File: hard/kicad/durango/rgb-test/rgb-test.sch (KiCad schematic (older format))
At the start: 21 parts, among them J1 SCART, SW1 TEST, U1 74HCT4040, U18 74HC85, U2 74HC4040, U20 74HC85, U3 74HC21, U4 74HC02, U5 74HC245, U6 74HC86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

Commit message: annotate and improve RGB tester
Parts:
- R4: value 1K -> 1K2
- R5: value 150 -> 180
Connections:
- net +5V: now also U3.13; no longer U3.1
- net FEND: now also U3.6; no longer U3.8
- net H2: now also U3.9; no longer U3.2
- net LEND: now also U3.8; no longer U3.6
- net S_G: now also J1.11 (Pin_11), R1.1; no longer J1.15 (Pin_15), R2.1
- net V0: now also U3.1; no longer U3.13
- net VA1: now also U3.12; no longer U3.5
- net ~DEH: now also U3.10; no longer U3.4
- net ~DEV: now also U3.4; no longer U3.10
- net at U2.5 (Q3), U20.12 (A1): now also U3.5; no longer U3.9
- net at U2.3 (Q4), U20.13 (A2): now also U3.2; no longer U3.12
- net FB: now reaches J1.16 (Pin_16), SW1.1 (A)
- new net S_R: J1.15 (Pin_15), R2.1
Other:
- note added: "74AC might be fast enough for nominal f."
- note added: "Horizontal/Vertical pattern choice,\nmay be connected to any counter output"
- note added: "may be supressed,\nfor buffering only"
- note added: "or +5V for\nnominal f."
- note added: "or 24 MHz\nfor nominal f."
- note added: "or higher,\nup to 360"
- note added: "or lower, down to 470 ohm"
- note added: "press to disable RGB\n(dark grey square)"
- note added: "these may be supressed,\nfor buffering only"
- moved on the sheet: U3A, U3B
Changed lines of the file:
@@
 L power:+5V #PWR0120
 U 1 1 6080689B
-P 4650 3900
-F 0 "#PWR0120" H 4650 3750 50  0001 C CNN
-F 1 "+5V" V 4700 3950 50  0000 L CNN
-F 2 "" H 4650 3900 50  0001 C CNN
-F 3 "" H 4650 3900 50  0001 C CNN
-	1    4650 3900
-	0    -1   -1   0
+P 4650 3300
+F 0 "#PWR0120" H 4650 3150 50  0001 C CNN
+F 1 "+5V" H 4700 3350 50  0000 L CNN
+F 2 "" H 4650 3300 50  0001 C CNN
+F 3 "" H 4650 3300 50  0001 C CNN
+	1    4650 3300
+	1    0    0    -1
 $EndComp
 $Comp
@@
 P 6800 5200
 F 0 "R4" V 6700 5200 50  0000 C CNN
-F 1 "1K" V 6800 5200 50  0000 C CNN
+F 1 "1K2" V 6800 5200 50  0000 C CNN
 F 2 "Resistor_THT:R_Axial_DIN0207_L6.3mm_D2.5mm_P2.54mm_Vertical" V 6730 5200 50  0001 C CNN
 F 3 "~" H 6800 5200 50  0001 C CNN
@@
 U 1 1 615F5223
 P 8950 5700
-F 0 "R5" V 9050 5700 50  0000 C CNN
-F 1 "150" V 8950 5700 50  0000 C CNN
+F 0 "R5" V 8850 5700 50  0000 C CNN
+F 1 "180" V 8950 5700 50  0000 C CNN
 F 2 "Resistor_THT:R_Axial_DIN0309_L9.0mm_D3.2mm_P2.54mm_Vertical" V 8880 5700 50  0001 C CNN
 F 3 "~" H 8950 5700 50  0001 C CNN
@@
 Wire Wire Line
 	9950 2550 9750 2550
-Wire Wire Line
-	4300 2450 5450 2450
-Wire Wire Line
-	5450 2450 5450 3400
 Wire Wire Line
 	4650 4400 4950 4400
@@
 $EndComp
 Wire Wire Line
-	3600 2750 4100 2750
-Text Label 3800 2750 0    50   ~ 0
+	3600 2550 4250 2550
+Text Label 3800 2550 0    50   ~ 0
 VA1
-Wire Wire Line
-	3600 2550 5650 2550
-Connection ~ 5650 2550
 Wire Wire Line
 	3600 2650 5750 2650
@@
 Text Label 3800 2650 0    50   ~ 0
 ~LINE
-Text Label 3800 2550 0    50   ~ 0
+Text Label 3800 2750 0    50   ~ 0
 VA5
 Wire Wire Line
@@
 L 74xx:74LS21 U3
 U 1 1 615D7357
+P 7600 3800
+F 0 "U3" V 7700 3550 50  0000 C CNN
+F 1 "74HC21" V 7800 3550 50  0000 C CNN
+F 2 "Package_DIP:DIP-14_W7.62mm_Socket" H 7600 3800 50  0001 C CNN
+F 3 "http://www.ti.com/lit/gpn/sn74LS21" H 7600 3800 50  0001 C CNN
+	1    7600 3800
+	0    1    1    0
+$EndComp
+$Comp
+L 74xx:74LS21 U3
+U 2 1 615EA142
 P 3300 2600
-F 0 "U3" H 3550 2550 50  0000 C CNN
-F 1 "74HC21" H 3550 2450 50  0000 C CNN
+F 0 "U3" H 3600 2750 50  0000 R CNN
+F 1 "74HC21" H 3650 2850 50  0000 R CNN
 F 2 "Package_DIP:DIP-14_W7.62mm_Socket" H 3300 2600 50  0001 C CNN
 F 3 "http://www.ti.com/lit/gpn/sn74LS21" H 3300 2600 50  0001 C CNN
-	1    3300 2600
-	-1   0    0    -1
-$EndComp
-$Comp
-L 74xx:74LS21 U3
-U 2 1 615EA142
-P 7600 3800
-F 0 "U3" V 7650 4200 50  0000 R CNN
-F 1 "74HC21" V 7750 4200 50  0000 R CNN
-F 2 "Package_DIP:DIP-14_W7.62mm_Socket" H 7600 3800 50  0001 C CNN
-F 3 "http://www.ti.com/lit/gpn/sn74LS21" H 7600 3800 50  0001 C CNN
-	2    7600 3800
-	0    -1   1    0
+	2    3300 2600
+	-1   0    0    1
 $EndComp
 Wire Wire Line
@@
 NoConn ~ 2500 1100
 Wire Wire Line
-	2500 1600 4100 1600
-Wire Wire Line
-	4100 1600 4100 2750
-Wire Wire Line
-	2500 1800 4300 1800
-Wire Wire Line
-	4300 1800 4300 2450
+	2500 1600 4250 1600
+Wire Wire Line
+	4250 1600 4250 2550
+Wire Wire Line
+	2500 1800 5450 1800
 Wire Wire Line
 	2500 1900 5550 1900
@@
 Wire Wire Line
 	2500 2000 5650 2000
-Wire Wire Line
-	5650 2000 5650 2550
 Wire Wire Line
 	2500 2100 5750 2100
@@
 	5750 2100 5750 2150
 NoConn ~ 2500 2200
-Wire Wire Line
-	5650 2550 5650 3400
 Connection ~ 2000 800
 Wire Wire Line
@@
 Text Label 7550 5700 0    50   ~ 0
 S_R
-Text Label 7550 6000 0    50   ~ 0
+Text Label 7650 5900 1    50   ~ 0
 S_G
 Text Label 7550 6200 0    50   ~ 0
@@
 Text Label 8300 5500 0    50   ~ 0
 COMP
+Text Notes 8500 5050 0    50   ~ 0
+or lower, down to 470 ohm
+Text Notes 8700 5900 0    50   ~ 0
+or higher,\nup to 360
+Text Notes 3850 6400 0    50   ~ 10
+Horizontal/Vertical pattern choice,\nmay be connected to any counter output
+Text Notes 9300 2100 0    50   ~ 0
+may be supressed,\nfor buffering only
+Text Notes 3650 4650 0    50   ~ 0
+these may be supressed,\nfor buffering only
+Text Notes 500  1400 0    50   Italic 0
+or 24 MHz\nfor nominal f.
+Text Notes 3800 2450 0    50   Italic 0
+or +5V for\nnominal f.
+Wire Wire Line
+	5650 2000 5650 2750
+Wire Wire Line
+	5650 2750 3600 2750
+Connection ~ 5650 2750
+Wire Wire Line
+	5650 2750 5650 3400
+Wire Wire Line
+	5450 1800 5450 3400
+Text Notes 2300 750  0    50   Italic 0
+74AC might be fast enough for nominal f.
+Text Notes 8550 5550 0    50   ~ 10
+press to disable RGB\n(dark grey square)
+Text Label 8350 5700 0    50   ~ 0
+FB
+Connection ~ 4650 3300
 $EndSCHEMATC

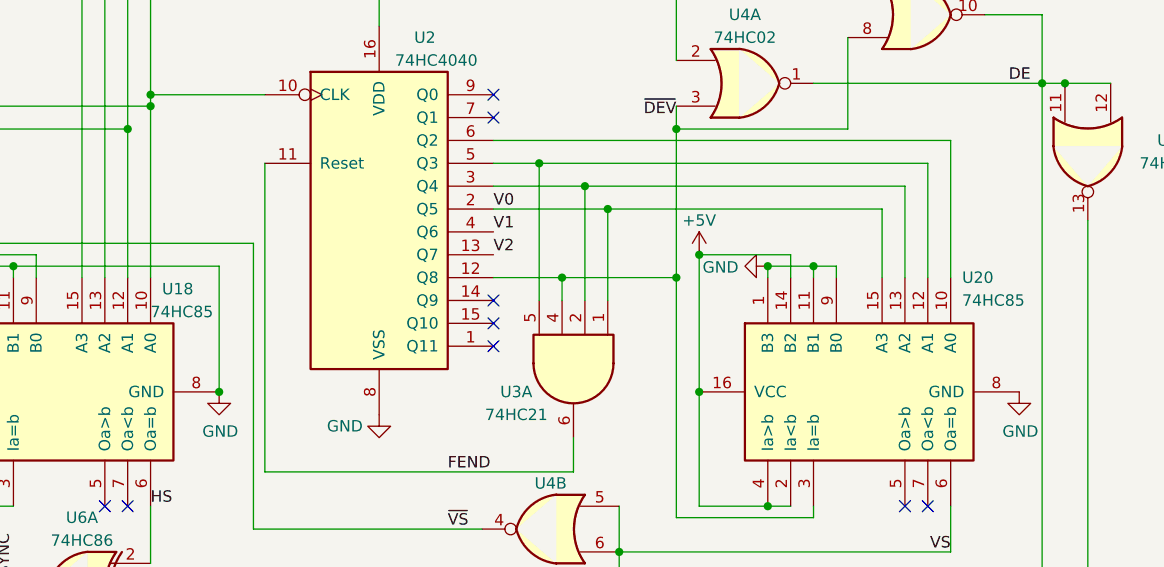
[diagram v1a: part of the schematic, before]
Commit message: rename HC85 from RGB tester
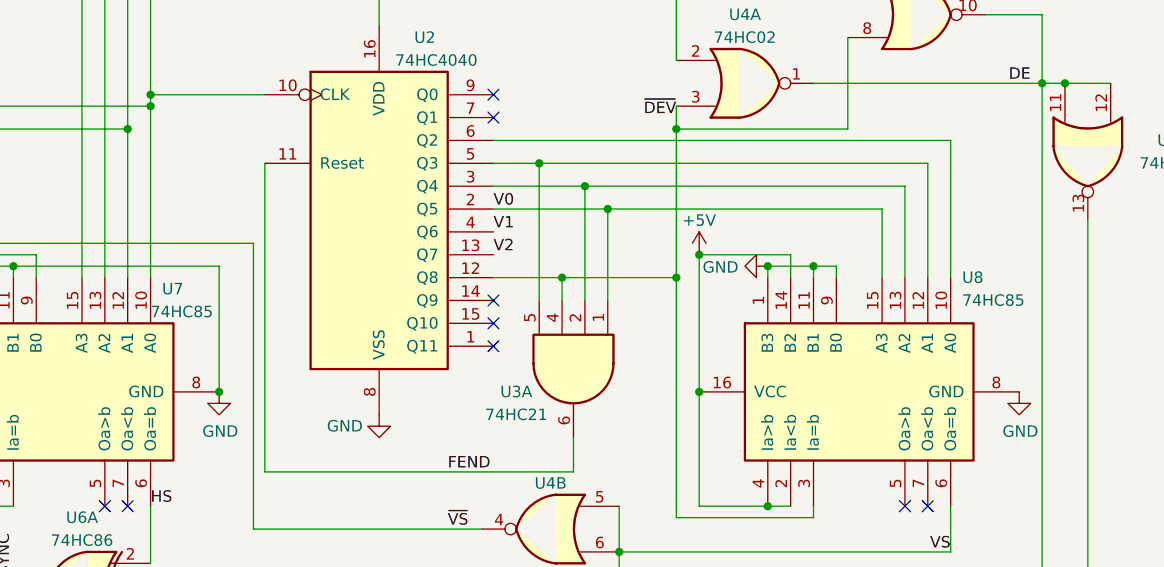
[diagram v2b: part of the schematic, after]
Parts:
- renumbered U18 to U7, U20 to U8
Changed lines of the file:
@@
 $EndComp
 $Comp
-L 74xx:74LS85 U18
+L 74xx:74LS85 U7
 U 1 1 607EF60C
 P 5350 3900
-F 0 "U18" V 4900 3450 50  0000 R CNN
+F 0 "U7" V 4900 3450 50  0000 R CNN
 F 1 "74HC85" V 5000 3500 50  0000 R CNN
 F 2 "Package_DIP:DIP-16_W7.62mm_Socket" H 5350 3900 50  0001 C CNN
@@
 $EndComp
 $Comp
-L 74xx:74LS85 U20
+L 74xx:74LS85 U8
 U 1 1 607F05F3
 P 8850 3900
-F 0 "U20" V 8350 3450 50  0000 R CNN
+F 0 "U8" V 8350 3450 50  0000 R CNN
 F 1 "74HC85" V 8450 3450 50  0000 R CNN
 F 2 "Package_DIP:DIP-16_W7.62mm_Socket" H 8850 3900 50  0001 C CNN

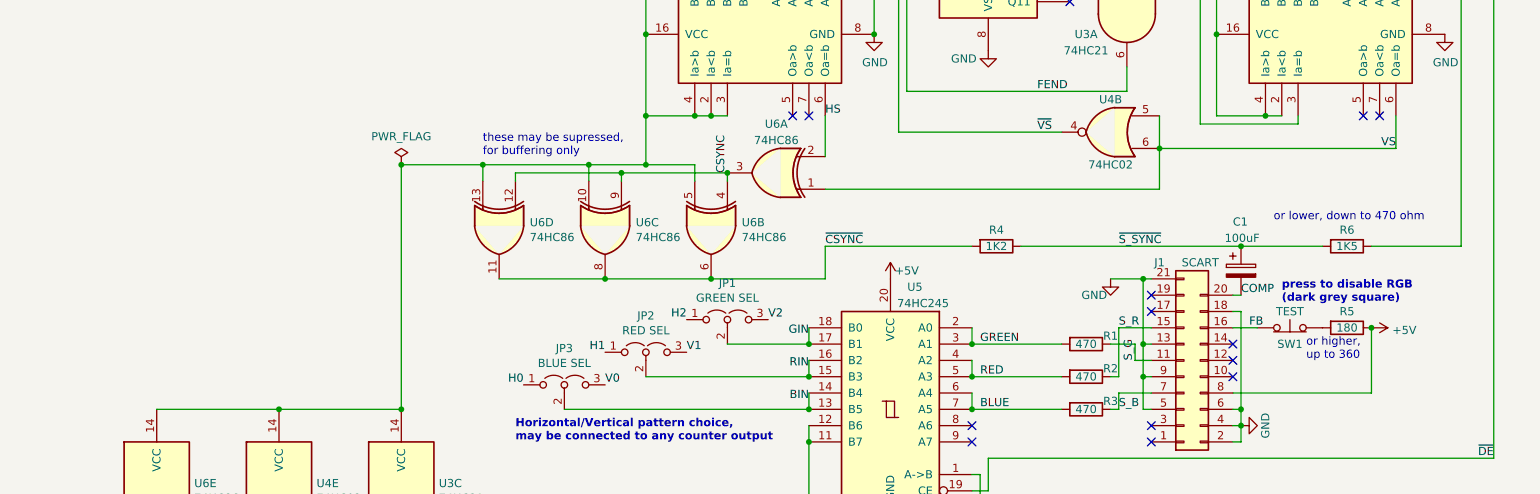
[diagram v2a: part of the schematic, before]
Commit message: PCB for RGB tester
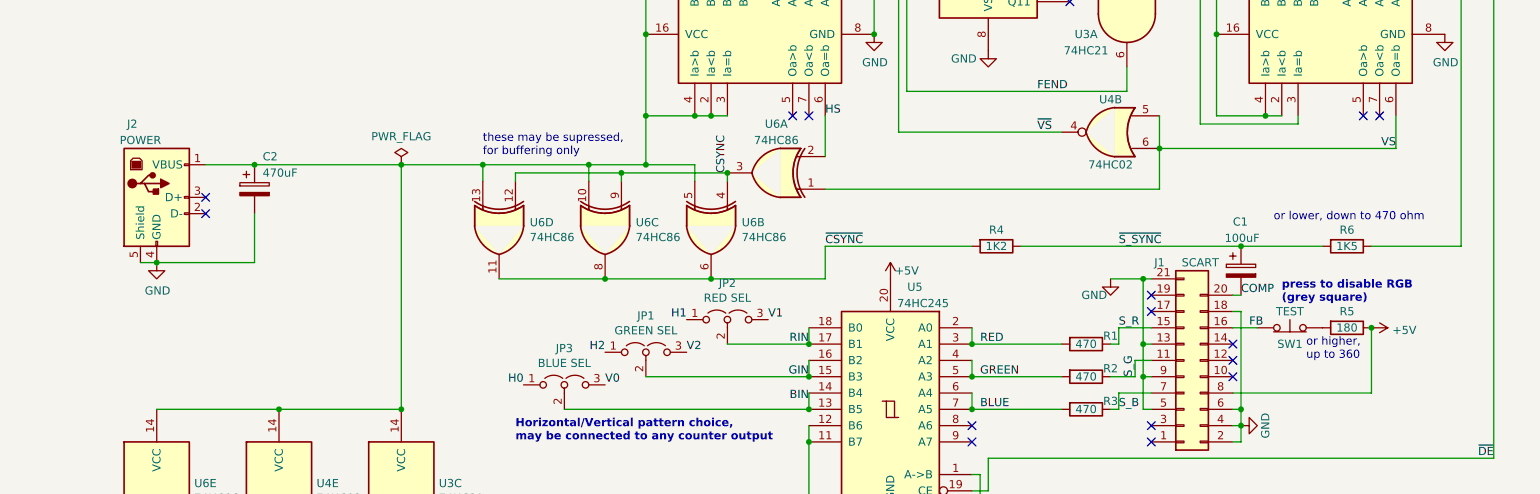
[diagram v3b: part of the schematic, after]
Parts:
- added C2: 470uF, Capacitor_THT:CP_Radial_D6.3mm_P2.50mm, symbol Device:CP
- added J2: POWER, Connector_USB:USB_B_OST_USB-B1HSxx_Horizontal, symbol Connector:USB_B
- JP1, JP2, JP3: footprint (none) -> Connector_PinHeader_2.54mm:PinHeader_1x03_P2.54mm_Vertical
- R6: footprint (none) -> Resistor_THT:R_Axial_DIN0207_L6.3mm_D2.5mm_P2.54mm_Vertical
- SW1: footprint (none) -> Button_Switch_THT:SW_PUSH_6mm
- U3, U4, U6: footprint (none) -> Package_DIP:DIP-14_W7.62mm_Socket
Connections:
- net +5V: now also C2.1, J2.1 (VBUS)
- net GIN: now also U5.15 (B3), U5.16 (B2); no longer U5.17 (B1), U5.18 (B0)
- net GND: now also C2.2, J2.4 (GND), J2.5 (Shield)
- net GREEN: now also R2.2, U5.4 (A2), U5.5 (A3); no longer R1.2, U5.2 (A0), U5.3 (A1)
- net RED: now also R1.2, U5.2 (A0), U5.3 (A1); no longer R2.2, U5.4 (A2), U5.5 (A3)
- net RIN: now also U5.17 (B1), U5.18 (B0); no longer U5.15 (B3), U5.16 (B2)
- net S_G: now also R2.1; no longer R1.1
- net S_R: now also R1.1; no longer R2.1
- no-connect marks 25 -> 27
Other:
- note added: "press to disable RGB\n(grey square)"
- note removed: "press to disable RGB\n(dark grey square)"
- moved on the sheet: JP1, JP2
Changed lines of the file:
@@
 	7550 5700 7750 5700
-Wire Wire Line
-	7650 5800 7500 5800
 Wire Wire Line
 	7650 5900 7750 5900
@@
 $EndComp
 Wire Wire Line
-	7650 5900 7650 5800
-Wire Wire Line
-	7550 5700 7550 6000
-Wire Wire Line
-	7550 6000 7500 6000
+	7650 5900 7650 6000
+Wire Wire Line
+	7650 6000 7500 6000
 Wire Wire Line
 	7550 6100 7550 6200
@@
 Wire Wire Line
 	9850 6500 9850 3150
+Text Label 6700 6000 0    50   ~ 0
+GREEN
 Text Label 6700 5800 0    50   ~ 0
-GREEN
-Text Label 6700 6000 0    50   ~ 0
 RED
 Text Label 6700 6200 0    50   ~ 0
@@
 Text Label 7550 5200 0    50   ~ 0
 ~S_SYNC
-Text Label 5650 5750 2    50   ~ 0
+Text Label 5650 6000 2    50   ~ 0
 GIN
-Text Label 5650 5950 2    50   ~ 0
+Text Label 5650 5800 2    50   ~ 0
 RIN
 Text Label 5650 6150 2    50   ~ 0
@@
 Text Label 7550 5700 0    50   ~ 0
 S_R
-Text Label 7650 5900 1    50   ~ 0
+Text Label 7650 6000 1    50   ~ 0
 S_G
 Text Label 7550 6200 0    50   ~ 0
@@
 F 0 "U6" H 5450 4450 50  0000 C CNN
 F 1 "74HC86" H 5450 4550 50  0000 C CNN
-F 2 "" H 5450 4750 50  0001 C CNN
+F 2 "Package_DIP:DIP-14_W7.62mm_Socket" H 5450 4750 50  0001 C CNN
 F 3 "http://www.ti.com/lit/gpn/sn74HC86" H 5450 4750 50  0001 C CNN
 	1    5450 4750
@@
 F 0 "U6" V 5004 5288 50  0000 L CNN
 F 1 "74HC86" V 5095 5288 50  0000 L CNN
-F 2 "" H 5050 5100 50  0001 C CNN
+F 2 "Package_DIP:DIP-14_W7.62mm_Socket" H 5050 5100 50  0001 C CNN
 F 3 "http://www.ti.com/lit/gpn/sn74HC86" H 5050 5100 50  0001 C CNN
 	2    5050 5100
@@
 F 0 "U6" V 4354 5288 50  0000 L CNN
 F 1 "74HC86" V 4445 5288 50  0000 L CNN
-F 2 "" H 4400 5100 50  0001 C CNN
+F 2 "Package_DIP:DIP-14_W7.62mm_Socket" H 4400 5100 50  0001 C CNN
 F 3 "http://www.ti.com/lit/gpn/sn74HC86" H 4400 5100 50  0001 C CNN
 	3    4400 5100
@@
 F 0 "U6" V 3704 5288 50  0000 L CNN
 F 1 "74HC86" V 3795 5288 50  0000 L CNN
-F 2 "" H 3750 5100 50  0001 C CNN
+F 2 "Package_DIP:DIP-14_W7.62mm_Socket" H 3750 5100 50  0001 C CNN
 F 3 "http://www.ti.com/lit/gpn/sn74HC86" H 3750 5100 50  0001 C CNN
 	4    3750 5100
@@
 F 0 "U6" H 1880 6746 50  0000 L CNN
 F 1 "74HC86" H 1880 6655 50  0000 L CNN
-F 2 "" H 1650 6700 50  0001 C CNN
+F 2 "Package_DIP:DIP-14_W7.62mm_Socket" H 1650 6700 50  0001 C CNN
 F 3 "http://www.ti.com/lit/gpn/sn74HC86" H 1650 6700 50  0001 C CNN
 	5    1650 6700
@@
 F 0 "U4" H 2630 6746 50  0000 L CNN
 F 1 "74HC02" H 2630 6655 50  0000 L CNN
-F 2 "" H 2400 6700 50  0001 C CNN
+F 2 "Package_DIP:DIP-14_W7.62mm_Socket" H 2400 6700 50  0001 C CNN
 F 3 "http://www.ti.com/lit/gpn/sn74hc02" H 2400 6700 50  0001 C CNN
 	5    2400 6700
@@
 F 0 "U3" H 3380 6746 50  0000 L CNN
 F 1 "74HC21" H 3380 6655 50  0000 L CNN
-F 2 "" H 3150 6700 50  0001 C CNN
+F 2 "Package_DIP:DIP-14_W7.62mm_Socket" H 3150 6700 50  0001 C CNN
 F 3 "http://www.ti.com/lit/gpn/sn74LS21" H 3150 6700 50  0001 C CNN
 	3    3150 6700
@@
 	3150 6200 3150 4700
 Wire Wire Line
-	3150 4700 3650 4700
+	3150 4700 2250 4700
 Connection ~ 3150 6200
 Connection ~ 2400 6200
@@
 F 0 "R6" V 8850 5200 50  0000 C CNN
 F 1 "1K5" V 8950 5200 50  0000 C CNN
-F 2 "" V 8880 5200 50  0001 C CNN
+F 2 "Resistor_THT:R_Axial_DIN0207_L6.3mm_D2.5mm_P2.54mm_Vertical" V 8880 5200 50  0001 C CNN
 F 3 "~" H 8950 5200 50  0001 C CNN
 	1    8950 5200
@@
 L Jumper:Jumper_3_Open JP1
 U 1 1 629CB504
+P 4650 5850
+F 0 "JP1" H 4650 6074 50  0000 C CNN
+F 1 "GREEN SEL" H 4650 5983 50  0000 C CNN
+F 2 "Connector_PinHeader_2.54mm:PinHeader_1x03_P2.54mm_Vertical" H 4650 5850 50  0001 C CNN
+F 3 "~" H 4650 5850 50  0001 C CNN
+	1    4650 5850
+	1    0    0    -1
+$EndComp
+$Comp
+L Jumper:Jumper_3_Open JP2
+U 1 1 629CE90F
 P 5150 5650
-F 0 "JP1" H 5150 5874 50  0000 C CNN
-F 1 "GREEN SEL" H 5150 5783 50  0000 C CNN
-F 2 "" H 5150 5650 50  0001 C CNN
+F 0 "JP2" H 5150 5874 50  0000 C CNN
+F 1 "RED SEL" H 5150 5783 50  0000 C CNN
+F 2 "Connector_PinHeader_2.54mm:PinHeader_1x03_P2.54mm_Vertical" H 5150 5650 50  0001 C CNN
 F 3 "~" H 5150 5650 50  0001 C CNN
 	1    5150 5650
-	1    0    0    -1
-$EndComp
-$Comp
-L Jumper:Jumper_3_Open JP2
-U 1 1 629CE90F
-P 4650 5850
-F 0 "JP2" H 4650 6074 50  0000 C CNN
-F 1 "RED SEL" H 4650 5983 50  0000 C CNN
-F 2 "" H 4650 5850 50  0001 C CNN
-F 3 "~" H 4650 5850 50  0001 C CNN
-	1    4650 5850
 	1    0    0    -1
 $EndComp
@@
 F 0 "JP3" H 4150 6274 50  0000 C CNN
 F 1 "BLUE SEL" H 4150 6183 50  0000 C CNN
-F 2 "" H 4150 6050 50  0001 C CNN
+F 2 "Connector_PinHeader_2.54mm:PinHeader_1x03_P2.54mm_Vertical" H 4150 6050 50  0001 C CNN
 F 3 "~" H 4150 6050 50  0001 C CNN
 	1    4150 6050
@@
 Text Label 3900 6050 2    50   ~ 0
 H0
+Text Label 4900 5650 2    50   ~ 0
+H1
 Text Label 4400 5850 2    50   ~ 0
-H1
-Text Label 4900 5650 2    50   ~ 0
 H2
 Text Label 4400 6050 0    50   ~ 0
 V0
+Text Label 5400 5650 0    50   ~ 0
+V1
 Text Label 4900 5850 0    50   ~ 0
-V1
-Text Label 5400 5650 0    50   ~ 0
 V2
 Connection ~ 5150 4750
@@
 F 0 "SW1" H 8600 5600 50  0000 C CNN
 F 1 "TEST" H 8600 5800 50  0000 C CNN
-F 2 "" H 8600 5900 50  0001 C CNN
+F 2 "Button_Switch_THT:SW_PUSH_6mm" H 8600 5900 50  0001 C CNN
 F 3 "~" H 8600 5900 50  0001 C CNN
 	1    8600 5700
@@
 74AC might be fast enough for nominal f.
 Text Notes 8550 5550 0    50   ~ 10
-press to disable RGB\n(dark grey square)
+press to disable RGB\n(grey square)
 Text Label 8350 5700 0    50   ~ 0
 FB
 Connection ~ 4650 3300
+Wire Wire Line
+	7550 5700 7550 5800
+Wire Wire Line
+	7550 5800 7500 5800
+$Comp
+L Connector:USB_B J2
+U 1 1 625936AB
+P 1650 4900
+F 0 "J2" H 1500 5350 50  0000 C CNN
+F 1 "POWER" H 1550 5250 50  0000 C CNN
+F 2 "Connector_USB:USB_B_OST_USB-B1HSxx_Horizontal" H 1800 4850 50  0001 C CNN
+F 3 " ~" H 1800 4850 50  0001 C CNN
+	1    1650 4900
+	1    0    0    -1
+$EndComp
+$Comp
+L power:GND #PWR0102
+U 1 1 625A1F95
+P 1650 5300
+F 0 "#PWR0102" H 1650 5050 50  0001 C CNN
+F 1 "GND" H 1655 5127 50  0000 C CNN
+F 2 "" H 1650 5300 50  0001 C CNN
+F 3 "" H 1650 5300 50  0001 C CNN
+	1    1650 5300
+	1    0    0    -1
+$EndComp
+Wire Wire Line
+	1550 5300 1650 5300
+Connection ~ 1650 5300
+NoConn ~ 1950 4900
+NoConn ~ 1950 5000
+$Comp
+L Device:CP C2
+U 1 1 62638BCA
+P 2250 4850
+F 0 "C2" H 2300 5050 50  0000 L CNN
+F 1 "470uF" H 2300 4950 50  0000 L CNN
+F 2 "Capacitor_THT:CP_Radial_D6.3mm_P2.50mm" H 2288 4700 50  0001 C CNN
+F 3 "~" H 2250 4850 50  0001 C CNN
+	1    2250 4850
+	1    0    0    -1
+$EndComp
+Connection ~ 2250 4700
+Wire Wire Line
+	1650 5300 2250 5300
+Wire Wire Line
+	2250 5300 2250 5000
+Wire Wire Line
+	3150 4700 3650 4700
+Wire Wire Line
+	2250 4700 1950 4700
 $EndSCHEMATC
